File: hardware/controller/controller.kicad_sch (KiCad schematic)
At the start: 28 parts, among them J1 Conn_02x15_Odd_Even, J10 conn_wifi, J11 conn_gpio, J2 Conn_01x20, J3 Conn_01x20, J4 Conn_01x02, J5 conn_vol, J6 conn_bl, J7 conn_br, J8 conn_dsp, J9 conn_i2s_mplx, SW1 RESET, U1 Display_5"_RA8875, U2 TSR_1-2433, U3 TSR_1-2433, U5 TSR_1-2433

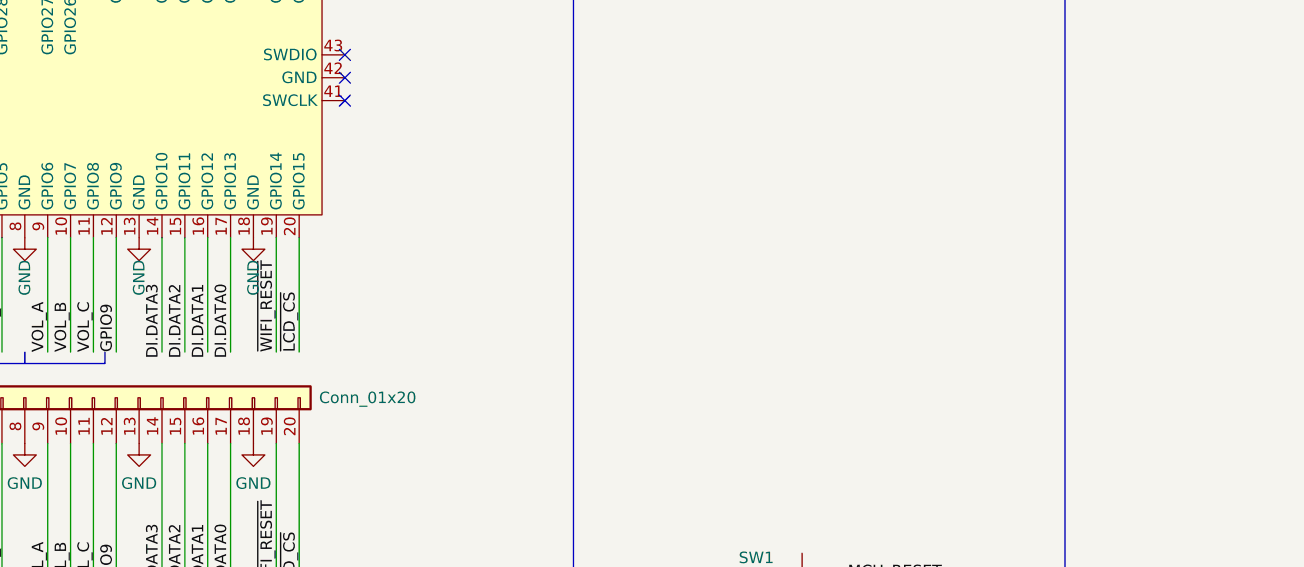
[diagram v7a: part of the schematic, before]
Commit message: Added corrections regarding the i2s-multiplexer interface
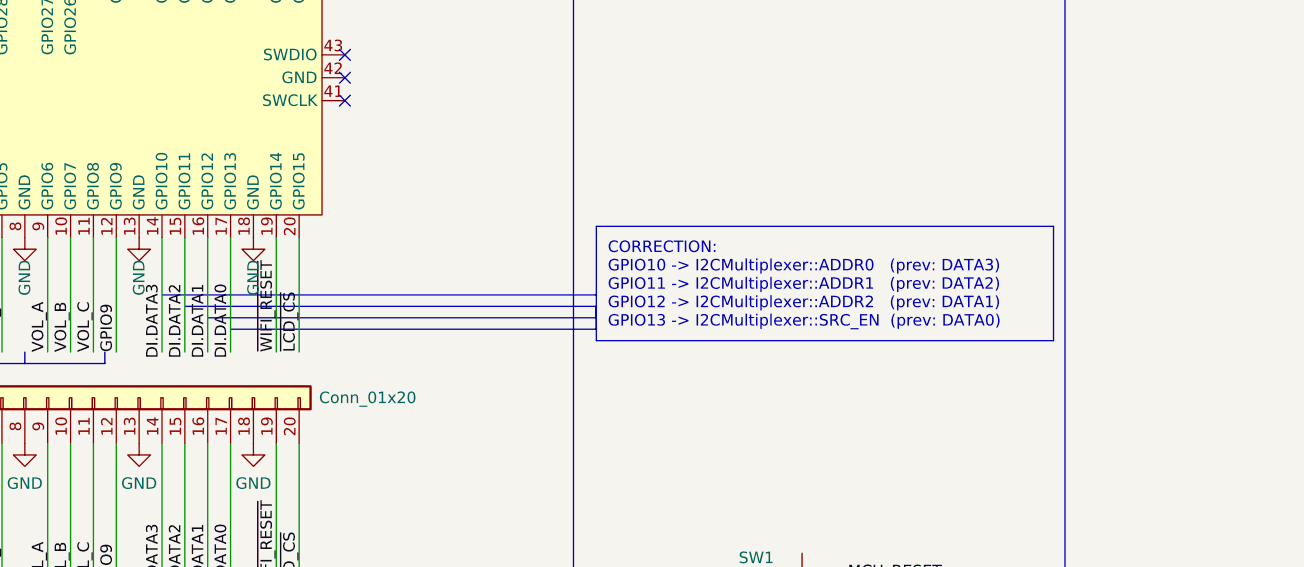
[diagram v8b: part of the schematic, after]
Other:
- note added: "CORRECTION: GPIO10 -> I2CMultiplexer::ADDR0 (prev: DATA3) GPIO11 -> I2CMultiplexer::ADDR1 (prev: DATA2) GPIO12 -> I2CMultiplexer::ADDR2 (prev: DATA1) GPIO13 -> I2CMultiplexer::SRC_EN (prev: DATA0)"
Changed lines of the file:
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@@
+    (stroke (width 0) (type default) (color 0 0 0 0))
+  )
+  (polyline (pts (xy 128.27 219.71) (xy 179.07 219.71))
     (stroke (width 0) (type default) (color 0 0 0 0))
   )
@@
     (stroke (width 0) (type default) (color 255 0 0 1))
   )
+  (polyline (pts (xy 85.09 229.87) (xy 128.27 229.87))
+    (stroke (width 0) (type default) (color 0 0 0 0))
+  )
   (wire (pts (xy 345.44 229.87) (xy 345.44 231.14))
     (stroke (width 0) (type default) (color 0 0 0 0))
@@
     (stroke (width 0) (type default) (color 0 0 0 0))
   )
+  (polyline (pts (xy 87.63 231.14) (xy 128.27 231.14))
+    (stroke (width 0) (type default) (color 0 0 0 0))
+  )
   (bus (pts (xy 125.73 128.27) (xy 125.73 267.97))
     (stroke (width 0) (type default) (color 0 0 0 0))
@@
   )
   (wire (pts (xy 317.5 92.71) (xy 337.82 92.71))
+    (stroke (width 0) (type default) (color 0 0 0 0))
+  )
+  (polyline (pts (xy 82.55 228.6) (xy 128.27 228.6))
+    (stroke (width 0) (type default) (color 0 0 0 0))
+  )
+  (polyline (pts (xy 128.27 229.87) (xy 128.27 228.6))
+    (stroke (width 0) (type default) (color 0 0 0 0))
+  )
+  (polyline (pts (xy 128.27 232.41) (xy 179.07 232.41))
     (stroke (width 0) (type default) (color 0 0 0 0))
   )
@@
     (stroke (width 0) (type default) (color 255 0 0 1))
   )
+  (polyline (pts (xy 80.01 227.33) (xy 128.27 227.33))
+    (stroke (width 0) (type default) (color 0 0 0 0))
+  )
   (wire (pts (xy 67.31 220.98) (xy 67.31 233.68))
+    (stroke (width 0) (type default) (color 0 0 0 0))
+  )
+  (polyline (pts (xy 179.07 232.41) (xy 179.07 219.71))
     (stroke (width 0) (type default) (color 0 0 0 0))
   )
@@
     (stroke (width 0) (type default) (color 0 0 0 0))
   )
+  (polyline (pts (xy 128.27 231.14) (xy 128.27 228.6))
+    (stroke (width 0) (type default) (color 0 0 0 0))
+  )
   (wire (pts (xy 54.61 220.98) (xy 54.61 233.68))
     (stroke (width 0) (type default) (color 0 0 0 0))
@@
   )
   (polyline (pts (xy 260.35 229.87) (xy 260.35 205.74))
+    (stroke (width 0) (type default) (color 0 0 0 0))
+  )
+  (polyline (pts (xy 128.27 219.71) (xy 128.27 232.41))
     (stroke (width 0) (type default) (color 0 0 0 0))
   )
@@
     (effects (font (size 1.27 1.27)) (justify left bottom))
   )
+  (text "CORRECTION:\nGPIO10 -> I2CMultiplexer::ADDR0   (prev: DATA3)\nGPIO11 -> I2CMultiplexer::ADDR1   (prev: DATA2)\nGPIO12 -> I2CMultiplexer::ADDR2   (prev: DATA1)\nGPIO13 -> I2CMultiplexer::SRC_EN  (prev: DATA0)"
+    (at 129.54 231.14 0)
+    (effects (font (size 1.27 1.27)) (justify left bottom))
+  )
